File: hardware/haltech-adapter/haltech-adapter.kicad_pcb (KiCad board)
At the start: 2 copper layers, 53.1 x 119 mm, 2 parts, among them J1 6437288-1, J2 Conn_02x32_Odd_Even

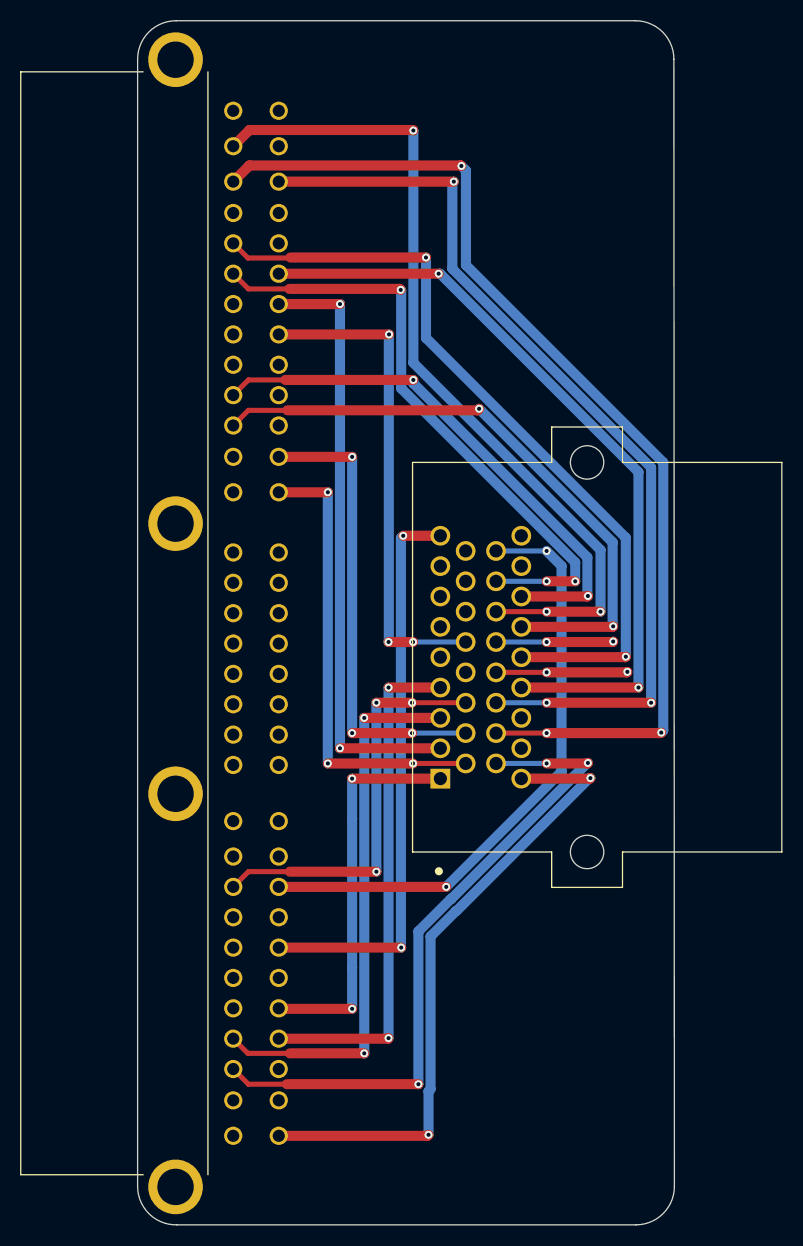
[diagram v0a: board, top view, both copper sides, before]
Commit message: Finish Haltech adapter
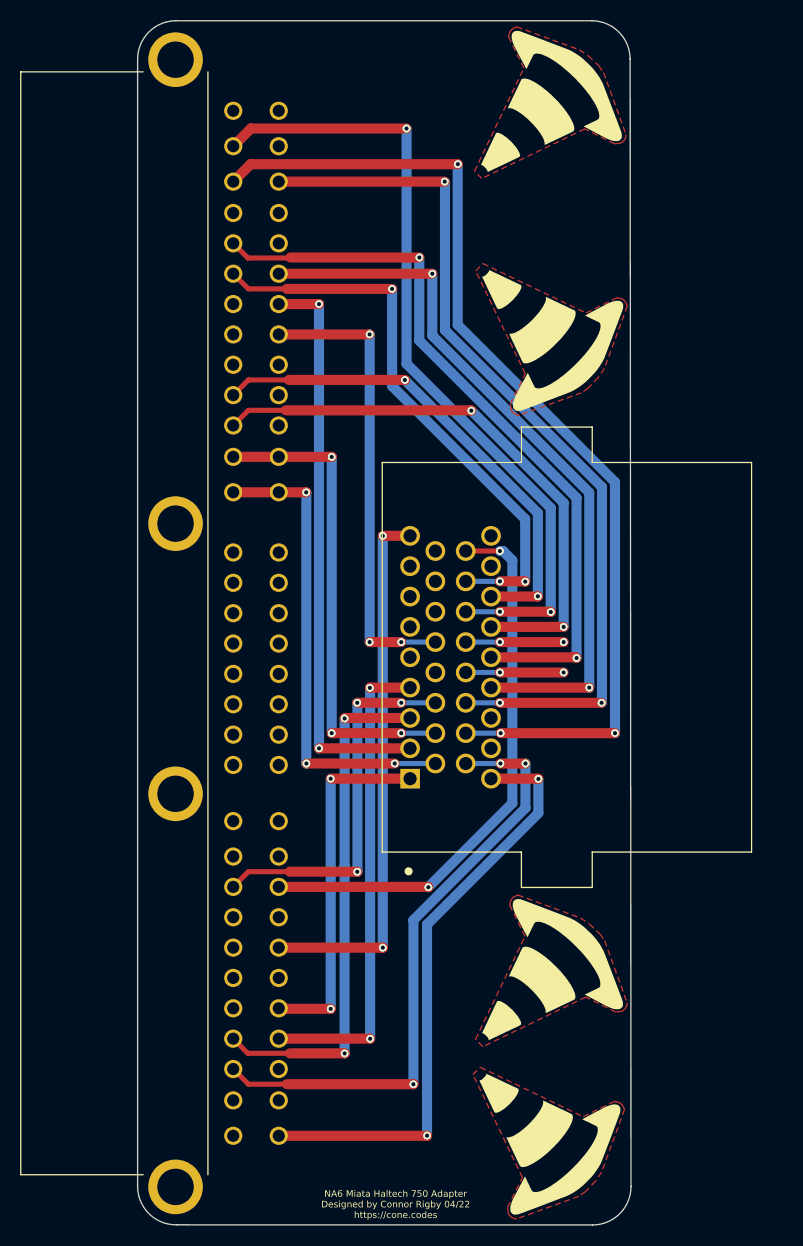
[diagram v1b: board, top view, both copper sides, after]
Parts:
- added G***: LOGO, logos:cone, F.Cu at (64.5, 43.0)
- added G***: LOGO, logos:cone, F.Cu at (64.3, 122.5)
- added G***: LOGO, logos:cone, F.Cu at (64.5, 108.2)
- added G***: LOGO, logos:cone, F.Cu at (64.4, 22.3)
- moved J1 2.99 mm to (55.9, 75.8)
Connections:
- net /DPI1 renamed /AC_IN
- net /DPO1 renamed /CEL
- net /FAN renamed /DPO4
- net /FUELP renamed /DPO5
- net /INJ1_3 renamed /INJ1
- net /MAP renamed /AVI3
- net /O2 renamed /AVI1
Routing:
- net /CEL: track 66.8 -> 60.6 mm
- net /INJ2: track 92.3 -> 87.7 mm
- net /TRIGGER+: track 61.1 -> 56.5 mm
- net /DPO4: track 60.1 -> 55.5 mm
- net /12V: track 63.7 -> 59.2 mm
- net /HOME+: track 53.5 -> 49.0 mm
- net /DPO5: track 61.0 -> 56.7 mm
- net /IAT: track 76.5 -> 72.2 mm
- net /CLT: track 77.7 -> 73.5 mm
- net /DPO3: track 84.0 -> 79.9 mm
- net /INJ1: track 103.9 -> 100.3 mm
- net /INJ3: track 13.0 -> 9.67 mm
- net /TPS: track 48.9 -> 45.9 mm
- net /IGN1: track 54.2 -> 51.2 mm
- net /AC_OUT: track 38.7 -> 35.8 mm
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- added copper zone on F.Cu, net (none)
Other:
- board size 53.1 x 119 mm -> 48.8 x 119 mm
- board text added: "NA6 Miata Haltech 750 Adapter Designed by Connor Rigby 04/22 https://cone.codes"
